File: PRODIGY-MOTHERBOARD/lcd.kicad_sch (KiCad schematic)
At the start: 2 parts, among them U13 PCF8574TS

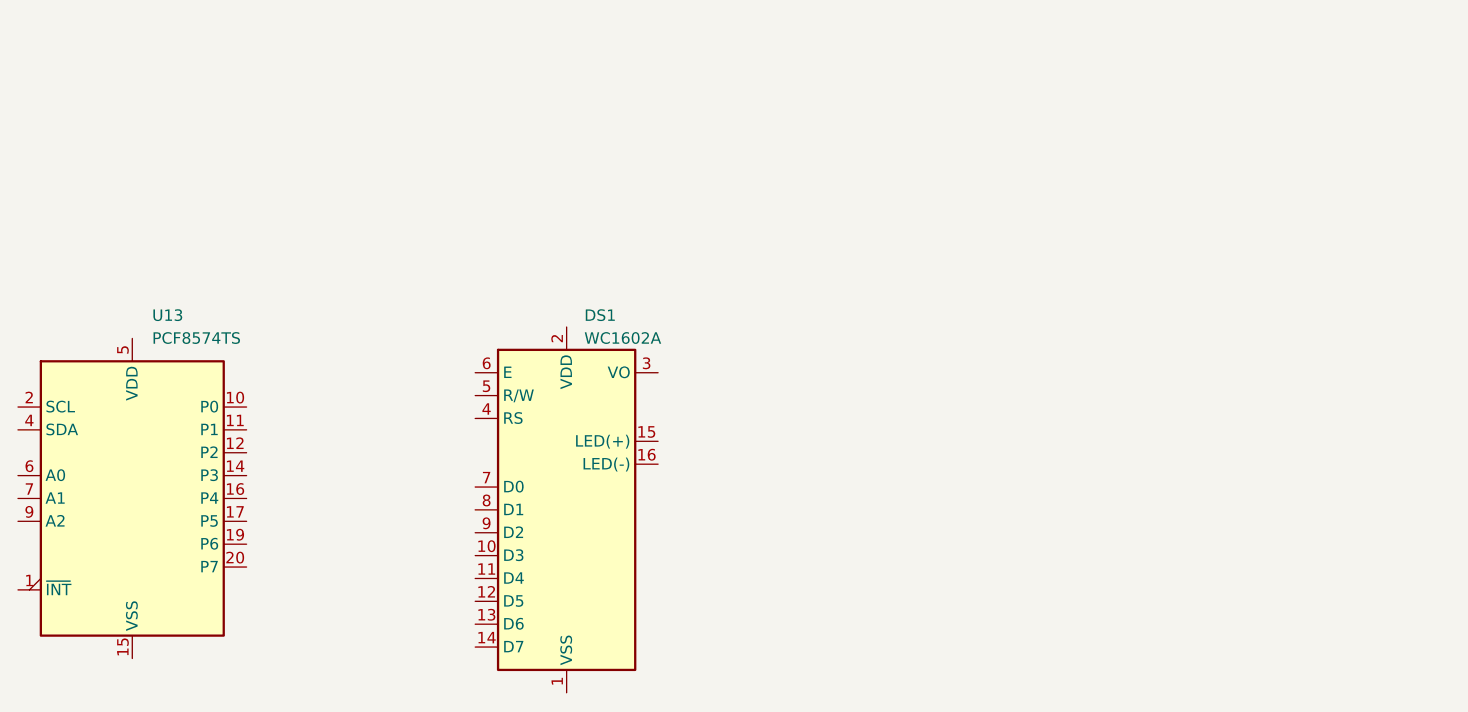
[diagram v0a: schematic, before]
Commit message: Finished I2C device and bus schematics. Added logic level translation.
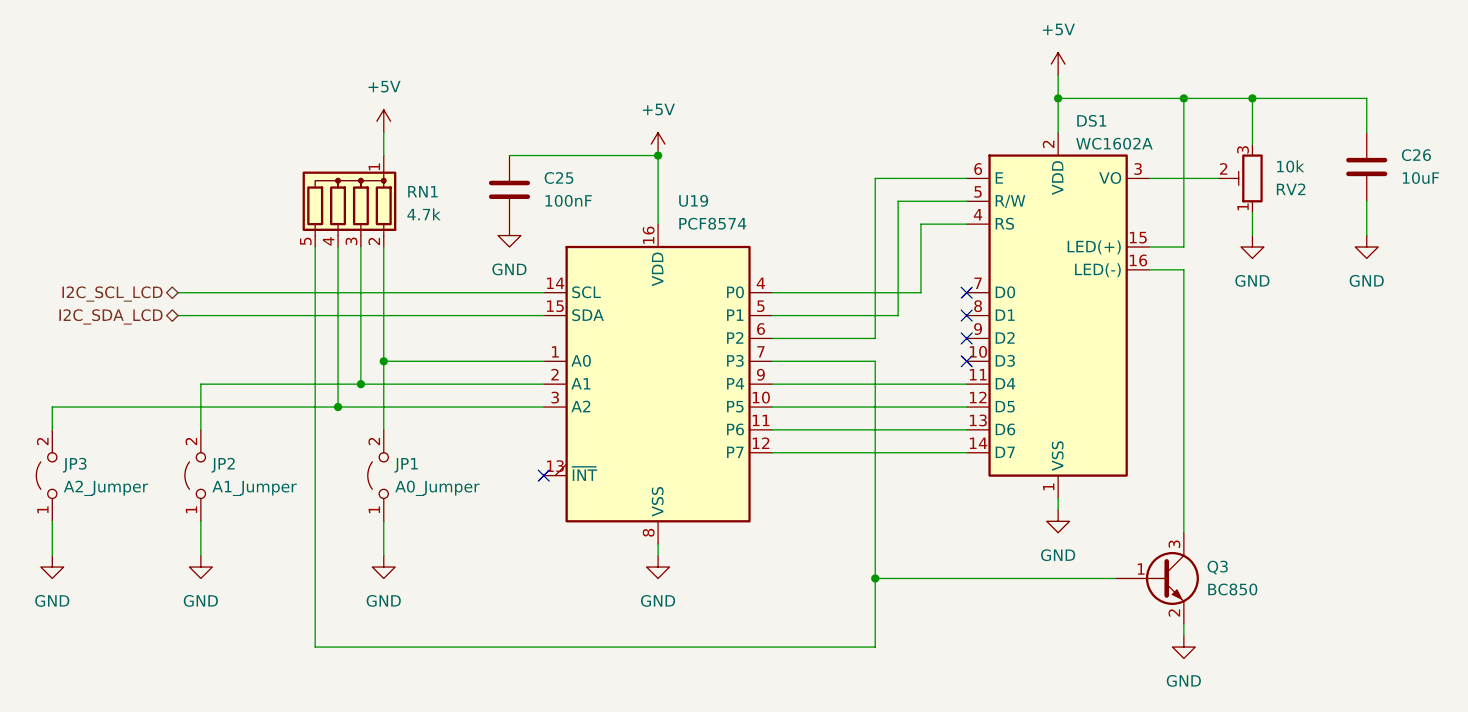
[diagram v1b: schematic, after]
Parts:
- removed U13: PCF8574TS, Package_SO:SSOP-20_4.4x6.5mm_P0.65mm, symbol Interface_Expansion:PCF8574TS
- added C25: 100nF, symbol Device:C
- added C26: 10uF, symbol Device:C
- added JP1: A0_Jumper, symbol Jumper:Jumper_2_Open
- added JP2: A1_Jumper, symbol Jumper:Jumper_2_Open
- added JP3: A2_Jumper, symbol Jumper:Jumper_2_Open
- added Q3: BC850, Package_TO_SOT_SMD:SOT-23, symbol Transistor_BJT:BC850
- added RN1: 4.7k, Resistor_SMD:R_Array_Convex_4x0603, symbol Device:R_Network04
- added RV2: 10k, Potentiometer_SMD:Potentiometer_Bourns_3224J_Horizontal, symbol Device:R_Potentiometer_Trim
- added U19: PCF8574, Package_SO:SSOP-20_4.4x6.5mm_P0.65mm, symbol Interface_Expansion:PCF8574
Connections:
- net GND: now reaches DS1.1 (VSS)
- net GND: now also C25.2, C26.2, JP1.1 (A), JP2.1 (A), JP3.1 (A), Q3.2 (E), RV2.1, U19.8 (VSS)
- net at DS1.11 (D4): now also U19.9 (P4)
- net at DS1.12 (D5): now also U19.10 (P5)
- net at DS1.13 (D6): now also U19.11 (P6)
- net at DS1.14 (D7): now also U19.12 (P7)
- net +5V: now reaches DS1.15 (LED(+))
- net +5V: now also DS1.2 (VDD), C25.1, C26.1, RN1.1 (common), RV2.3, U19.16 (VDD)
- net at DS1.16 (LED(-)): now also Q3.3 (C)
- net at DS1.3 (VO): now also RV2.2
- net at DS1.4 (RS): now also U19.4 (P0)
- net at DS1.5 (R/W): now also U19.5 (P1)
- net at DS1.6 (E): now also U19.6 (P2)
- new net: JP1.2 (B), RN1.2 (R1), U19.1 (A0)
- new net: JP2.2 (B), RN1.3 (R2), U19.2 (A1)
- new net: JP3.2 (B), RN1.4 (R3), U19.3 (A2)
- new net: Q3.1 (B), RN1.5 (R4), U19.7 (P3)
- new net I2C_SCL_LCD: U19.14 (SCL)
- new net I2C_SDA_LCD: U19.15 (SDA)
- no-connect marks 0 -> 5
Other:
- moved on the sheet: DS1
